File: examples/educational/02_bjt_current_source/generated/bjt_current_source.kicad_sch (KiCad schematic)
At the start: 6 parts, among them J1 9 V SUPPLY, J2 CURRENT OUTPUT, Q1 BC547, Q2 BC547

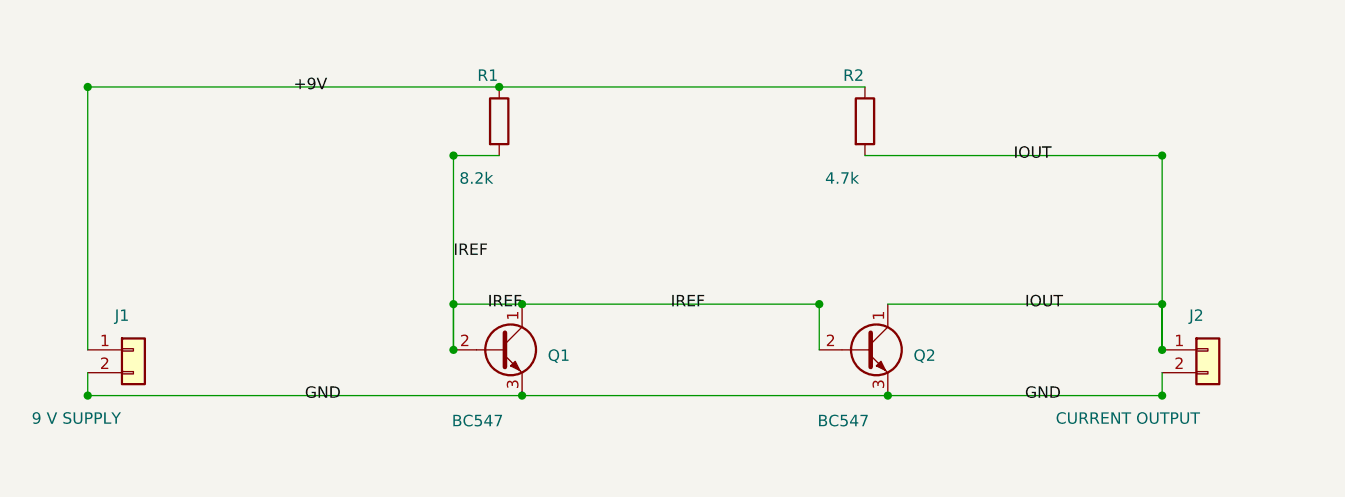
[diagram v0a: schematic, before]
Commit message: feat: infer conventional schematic topology layouts
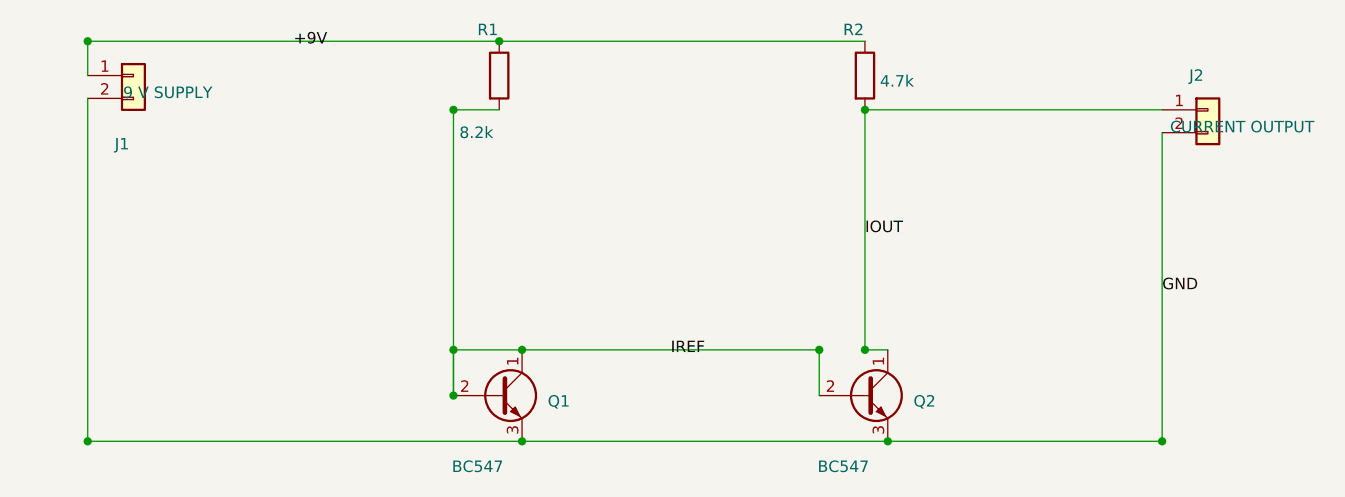
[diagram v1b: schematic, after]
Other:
- moved on the sheet: J1, J2, Q1, Q2, R1, R2
